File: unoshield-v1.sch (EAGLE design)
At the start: 24 parts, among them Q1 FDS5680, X1 SPRING-TERMINAL, X2 SPRING-TERMINAL

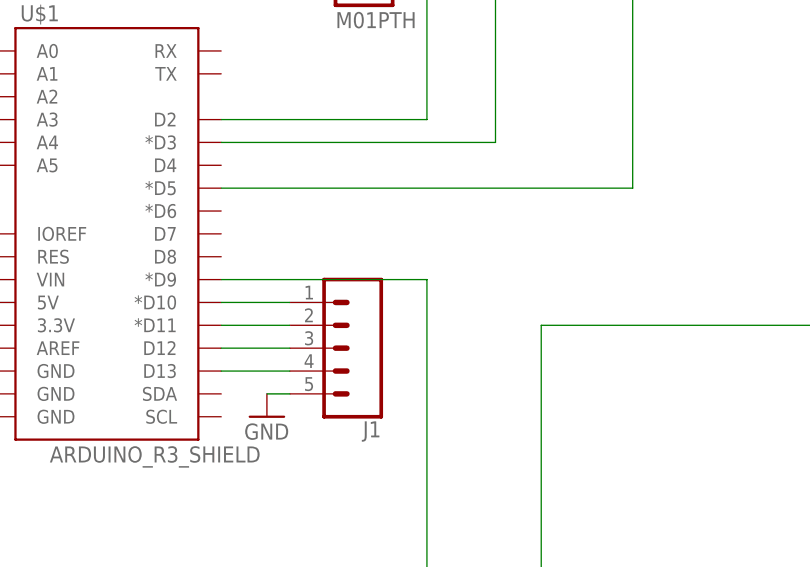
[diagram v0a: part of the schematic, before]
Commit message: added external digital I/O line
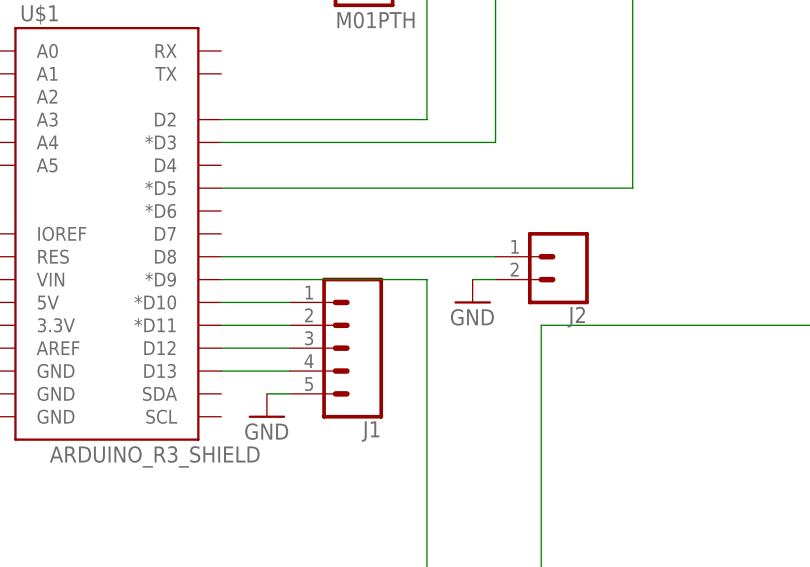
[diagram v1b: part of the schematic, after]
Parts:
- added J2: (no value), SparkFun-Connectors:CONN_02
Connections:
- new net N$13: J2.1, U$1.D8
- net GND: now also J2.2
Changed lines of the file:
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@@
 <part name="JP11" library="SparkFun-Connectors" deviceset="M01" device="PTH"/>
 <part name="JP12" library="SparkFun-Connectors" deviceset="M01" device="PTH"/>
+<part name="J2" library="SparkFun-Connectors" deviceset="CONN_02" device=""/>
+<part name="GND5" library="SparkFun-Aesthetics" deviceset="GND" device=""/>
 </parts>
 <sheets>
@@
 <instance part="JP11" gate="G$1" x="121.92" y="119.38"/>
 <instance part="JP12" gate="G$1" x="116.84" y="144.78" rot="R270"/>
+<instance part="J2" gate="G$1" x="144.78" y="88.9" rot="R180"/>
+<instance part="GND5" gate="1" x="134.62" y="83.82"/>
 </instances>
 <busses>
@@
 <pinref part="JP6" gate="G$1" pin="1"/>
 <junction x="104.14" y="139.7"/>
-<pinref part="JP6" gate="G$1" pin="1"/>
 </segment>
 <segment>
@@
 <wire x1="116.84" y1="137.16" x2="119.38" y2="137.16" width="0.1524" layer="91"/>
 <junction x="119.38" y="137.16"/>
+</segment>
+<segment>
+<pinref part="J2" gate="G$1" pin="2"/>
+<pinref part="GND5" gate="1" pin="GND"/>
+<wire x1="134.62" y1="86.36" x2="137.16" y2="86.36" width="0.1524" layer="91"/>
 </segment>
 </net>
@@
 </segment>
 </net>
+<net name="N$13" class="0">
+<segment>
+<pinref part="U$1" gate="G$1" pin="D8"/>
+<pinref part="J2" gate="G$1" pin="1"/>
+<wire x1="106.68" y1="88.9" x2="137.16" y2="88.9" width="0.1524" layer="91"/>
+</segment>
+</net>
